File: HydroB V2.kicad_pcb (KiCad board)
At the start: 4 copper layers, 74.7 x 90.4 mm, 61 parts, among them J1 EC sensor, J14 Screw_Terminal_01x02, J15 Screw_Terminal_01x02, J16 Screw_Terminal_01x02, J17 Screw_Terminal_01x02, J18 Screw_Terminal_01x02, J2 Screw_Terminal_01x02, J20 LCD, J21 DS18B20 sensor, J23 PH sensor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

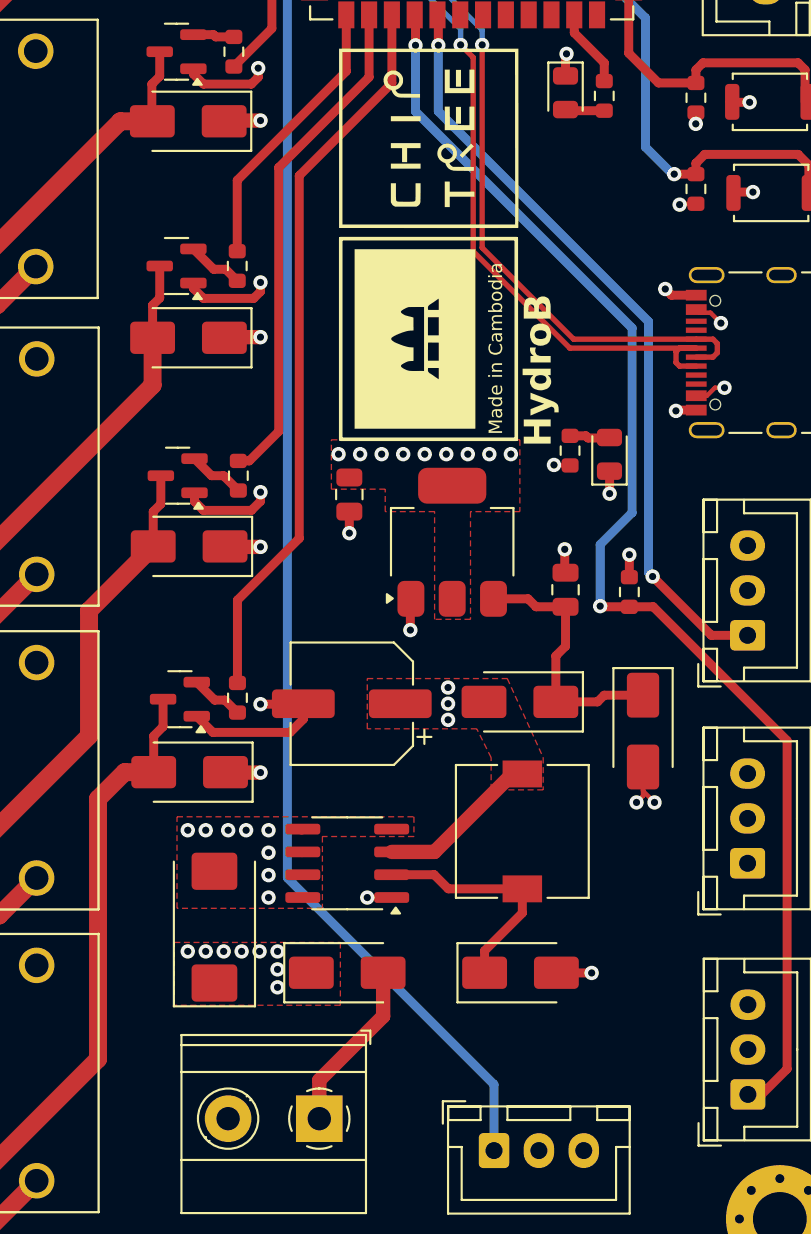
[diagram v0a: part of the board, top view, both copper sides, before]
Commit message: fixed VBUS connected to +12V
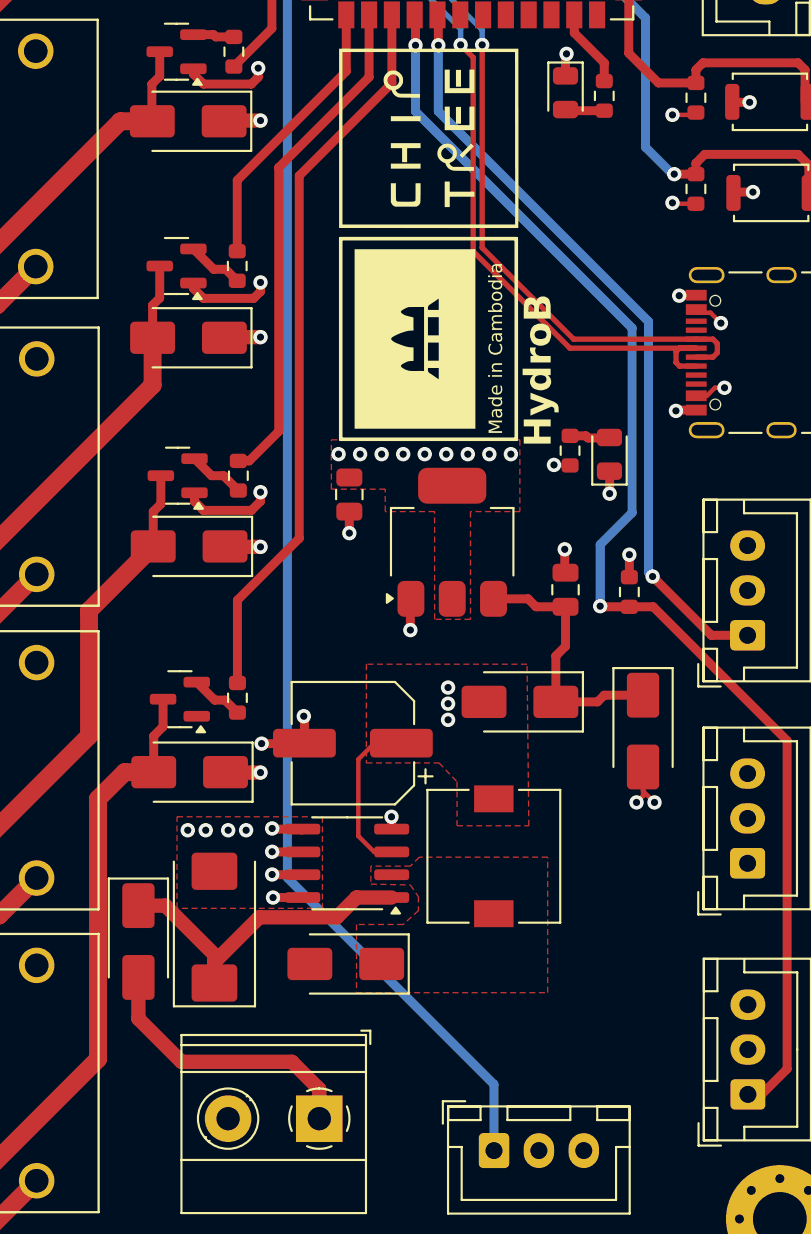
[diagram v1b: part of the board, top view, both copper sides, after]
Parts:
- moved D16 11.8 mm to (147.2, 123.0), turned to -90 degrees
- moved D17 9.75 mm to (158.8, 124.2), turned to 180 degrees
- moved C9 2.20 mm to (159.2, 111.9)
- moved L2 2.11 mm to (167.1, 118.2)
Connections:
- net Net-(D17-K) renamed /HydroB/Power Supply/OUT
- C8 pad 1: VBUS -> Net-(D16-K)
- D16 pad 1: VBUS -> Net-(D16-K)
- U4 pad 1: VBUS -> Net-(D16-K)
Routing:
- net Net-(D16-K): track 0.00 -> 19.5 mm
- net /HydroB/Power Supply/OUT: track 13.1 -> 0.00 mm
- net Net-(D16-A): track 9.60 -> 15.6 mm
- net VBUS: track 9.16 -> 7.81 mm, vias 13 -> 4
- net GND: track 58.0 -> 56.7 mm, vias 34 -> 35
- net +3.3V: track 7.27 -> 8.40 mm
- added copper zone on F.Cu, net /HydroB/Power Supply/OUT
- removed copper zone on F.Cu, net VBUS
